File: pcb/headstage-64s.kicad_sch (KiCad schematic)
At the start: 8 parts, among them J1 Conn_Coaxial, J2 DF40C-70DP-0.4V(51)

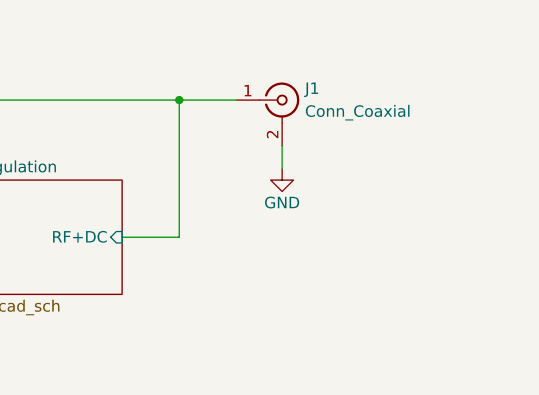
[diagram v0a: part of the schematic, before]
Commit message: Rev. A initial design prior to fab comments
- BOM simplification
- Added my initials to the board
- Made the board more easy to panlize
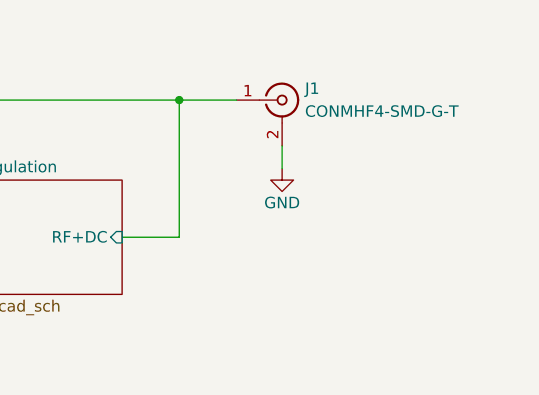
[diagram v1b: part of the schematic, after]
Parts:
- J1: value Conn_Coaxial -> CONMHF4-SMD-G-T; footprint jonnew:LINX_CONMHF4-SMD-G -> Headstage-64s:Coax-Adapter
- TP2: now left out of the parts list
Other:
- title: Headstage-RHS2116 -> Headstage-64s
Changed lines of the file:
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@@
   (paper "A4" portrait)
   (title_block
-    (title "Headstage-RHS2116")
-    (date "2021-12-16")
+    (title "Headstage-64s")
+    (date "2022-01-21")
     (rev "A")
     (company "Open Ephys, Inc")
@@
   )
   (symbol (lib_id "Connector:TestPoint") (at 52.07 60.96 0) (unit 1)
-    (in_bom yes) (on_board yes)
+    (in_bom no) (on_board yes)
     (property "Reference" "TP2" (id 0) (at 53.34 58.42 0)
       (effects (font (size 1.27 1.27)) (justify left))
@@
       (effects (font (size 1.27 1.27)) (justify left))
     )
-    (property "Value" "Conn_Coaxial" (id 1) (at 163.83 54.61 0)
-      (effects (font (size 1.27 1.27)) (justify left))
-    )
-    (property "Footprint" "jonnew:LINX_CONMHF4-SMD-G" (id 2) (at 161.29 53.34 0)
+    (property "Value" "CONMHF4-SMD-G-T" (id 1) (at 163.83 54.61 0)
+      (effects (font (size 1.27 1.27)) (justify left))
+    )
+    (property "Footprint" "Headstage-64s:Coax-Adapter" (id 2) (at 161.29 53.34 0)
       (effects (font (size 1.27 1.27)) hide)
     )
@@
       (reference "#PWR02") (unit 1) (value "+3.3V") (footprint "")
     )
+    (path "/ef67450c-7896-4369-9f65-a6a0bf770996/c8f58c2d-07ec-4355-92b4-a1615dc2f910"
+      (reference "#PWR03") (unit 1) (value "GND") (footprint "")
+    )
+    (path "/ef67450c-7896-4369-9f65-a6a0bf770996/21a98fd8-a677-4041-a72a-fa16dabfe8d3"
+      (reference "#PWR04") (unit 1) (value "+1V8") (footprint "")
+    )
     (path "/f805e42a-7731-4c63-aab8-b693117b73f1/f96f902c-692c-4845-9eef-cc912aa845ab"
       (reference "#PWR017") (unit 1) (value "GND") (footprint "")
@@
     )
     (path "/ef67450c-7896-4369-9f65-a6a0bf770996/111e9f78-ceab-42c3-b66c-e2ed604ec711"
-      (reference "C51") (unit 1) (value "1.0uF") (footprint "Capacitor_SMD:C_0402_1005Metric")
+      (reference "C51") (unit 1) (value "1uF") (footprint "Capacitor_SMD:C_0402_1005Metric")
     )
     (path "/ef67450c-7896-4369-9f65-a6a0bf770996/2b42fc13-7e16-4022-9298-19773a99f7dc"
-      (reference "C52") (unit 1) (value "1.0uF") (footprint "Capacitor_SMD:C_0402_1005Metric")
+      (reference "C52") (unit 1) (value "1uF") (footprint "Capacitor_SMD:C_0402_1005Metric")
     )
     (path "/ef67450c-7896-4369-9f65-a6a0bf770996/fcee6037-f9fd-4eff-9d73-c32d97d31ae2"
@@
     )
     (path "/ef67450c-7896-4369-9f65-a6a0bf770996/55545dfc-6930-4e99-9286-8901835b1e37"
-      (reference "D2") (unit 1) (value "LED") (footprint "jonnew:ROHM_SML-P11MTT86R")
+      (reference "D2") (unit 1) (value "SML-P11UTT86R") (footprint "jonnew:ROHM_SML-P11MTT86R")
     )
     (path "/ec2eb303-8bda-4887-86fa-cfe7bb147514/5e9fe99d-ee33-41ec-b2ff-8866abf981ee"
@@
     )
     (path "/9086d3ed-d48c-44a7-83ea-71ce6fdb9e26"
-      (reference "J1") (unit 1) (value "Conn_Coaxial") (footprint "jonnew:LINX_CONMHF4-SMD-G")
+      (reference "J1") (unit 1) (value "CONMHF4-SMD-G-T") (footprint "Headstage-64s:Coax-Adapter")
     )
     (path "/fccc0e4f-ed50-4339-ad4b-4dd5485914e2"
       (reference "J2") (unit 1) (value "DF40C-70DP-0.4V(51)") (footprint "jonnew:HIROSE_DF40C70DP04V51")
     )
+    (path "/ef67450c-7896-4369-9f65-a6a0bf770996/d1a6949e-04d4-4c1c-b488-f7d497860452"
+      (reference "J3") (unit 1) (value "SBH11-PBPC-D05-ST-BK") (footprint "Connector_IDC:IDC-Header_2x05_P2.54mm_Vertical")
+    )
     (path "/ef67450c-7896-4369-9f65-a6a0bf770996/b1fef073-48b9-4936-be2b-7ec71e5f6dd4"
       (reference "J5") (unit 1) (value "PINHD-1x7_ONIXJTAG-RevA") (footprint "jonnew:ONIXJTAG-RevA")
     )
+    (path "/ef67450c-7896-4369-9f65-a6a0bf770996/4a2bdb04-11f3-4675-8736-8b6d29b5959b"
+      (reference "JP1") (unit 1) (value "Jumper_2_Open") (footprint "jonnew:OE_SolderJumper-2_0201_Open_Pad")
+    )
     (path "/6a107470-4fd1-4a6d-84fa-4453722c41a9/63ea2017-127c-47a0-ae03-040ce3a6283c"
       (reference "L1") (unit 1) (value "BLM15AX102SN1D") (footprint "Inductor_SMD:L_0402_1005Metric")
@@
     )
     (path "/6a107470-4fd1-4a6d-84fa-4453722c41a9/a20bf941-be10-4b9f-bf67-16c9e833102b"
-      (reference "R3") (unit 1) (value "?") (footprint "Resistor_SMD:R_0201_0603Metric")
+      (reference "R3") (unit 1) (value "39.2,1%") (footprint "Resistor_SMD:R_0201_0603Metric")
     )
     (path "/6a107470-4fd1-4a6d-84fa-4453722c41a9/66966924-f4e3-42e3-b604-4f625989070c"
-      (reference "R4") (unit 1) (value "?") (footprint "Resistor_SMD:R_0201_0603Metric")
+      (reference "R4") (unit 1) (value "78.7k,1%") (footprint "Resistor_SMD:R_0201_0603Metric")
     )
     (path "/6a107470-4fd1-4a6d-84fa-4453722c41a9/8f2ed134-eb1d-4a2c-b225-1ddae1540dc0"
@@
     )
     (path "/6a107470-4fd1-4a6d-84fa-4453722c41a9/b7fbf054-a4bb-464c-87a8-918d57bd9d6d"
-      (reference "R6") (unit 1) (value "?") (footprint "Resistor_SMD:R_0201_0603Metric")
+      (reference "R6") (unit 1) (value "40.2k,1%") (footprint "Resistor_SMD:R_0201_0603Metric")
     )
     (path "/f805e42a-7731-4c63-aab8-b693117b73f1/9bdb9eb7-4e1a-4718-a0a3-e80ccfd63967"

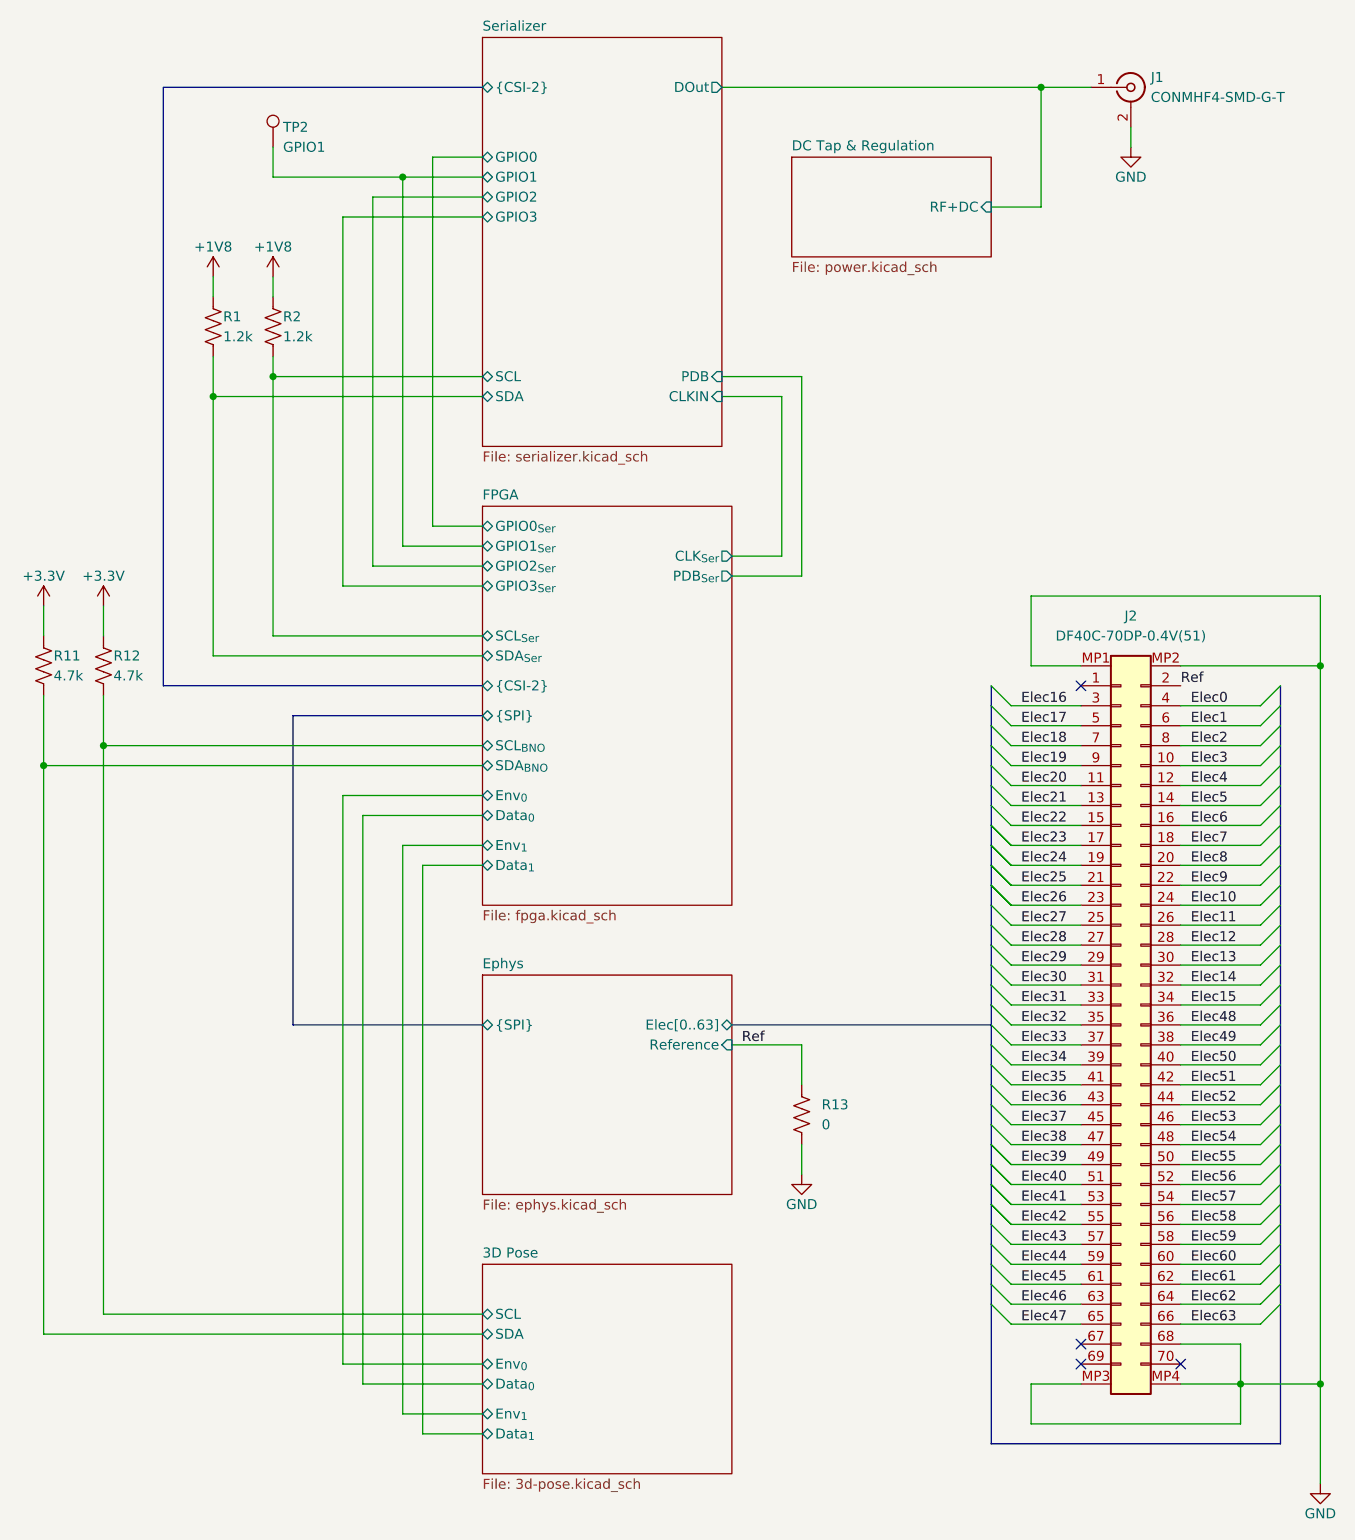
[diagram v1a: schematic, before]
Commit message: Small changes before speedy fabrication
- This is revision A
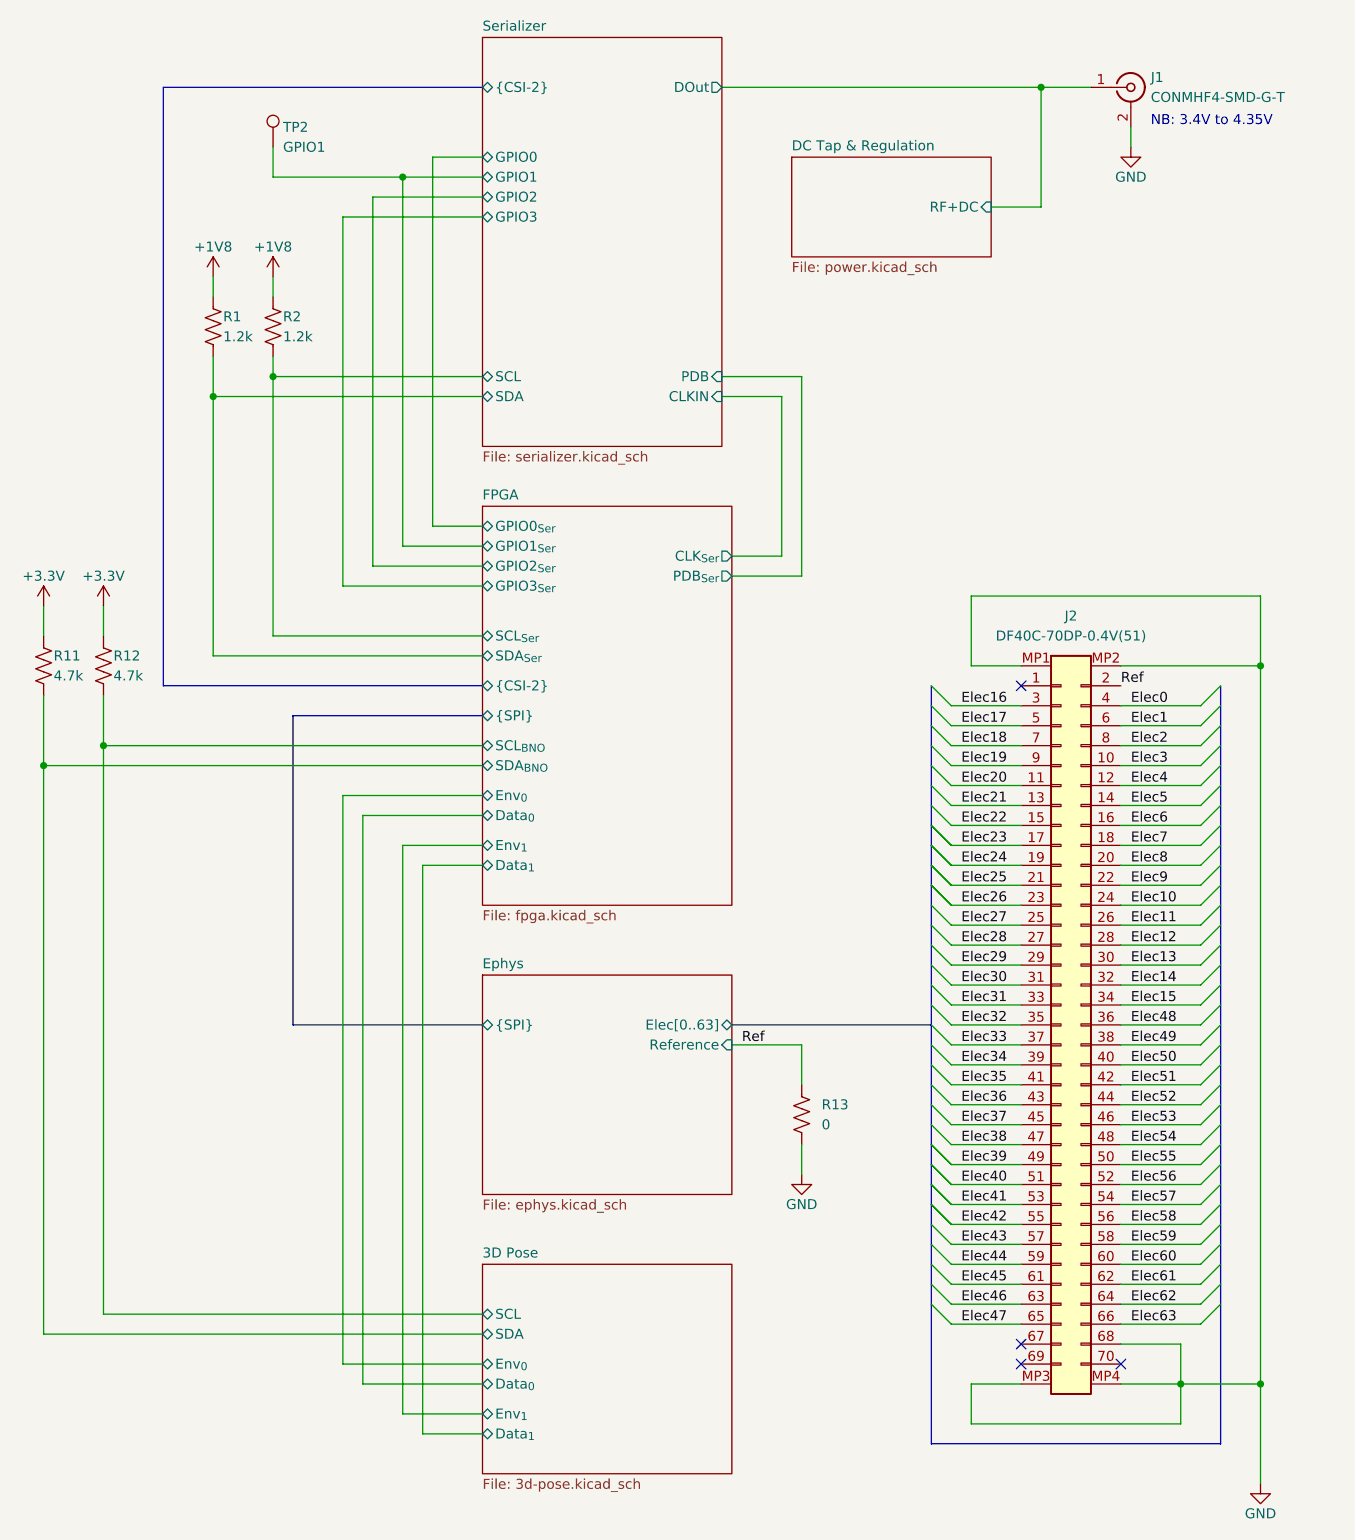
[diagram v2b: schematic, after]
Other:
- note added: "NB: 3.4V to 4.35V"
- moved on the sheet: J2

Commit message: Start of revision B
- Address the following issues
1. The photodiode anode is on pin 3, not pin 2
2. No paste on coax connector
3. CRESET_B needs to come out to programming header
4. Need PU on CS line.
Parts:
- J1, TP2: DNP (none) -> DNP
- R1, R2: value 1.2k -> 1k
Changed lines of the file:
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@@
     (title "Headstage-64s")
     (date "2022-01-21")
-    (rev "A")
+    (rev "B")
     (company "Open Ephys, Inc")
     (comment 1 "Jonathan P. Newman")
@@
       (effects (font (size 1.27 1.27)) hide)
     )
+    (property "DNP" "DNP" (id 4) (at 52.07 60.96 0)
+      (effects (font (size 1.27 1.27)) hide)
+    )
     (pin "1")
   )
@@
       (effects (font (size 1.27 1.27)) (justify left))
     )
-    (property "Value" "1.2k" (id 1) (at 45.72 85.09 0)
+    (property "Value" "1k" (id 1) (at 45.72 85.09 0)
       (effects (font (size 1.27 1.27)) (justify left))
     )
@@
       (effects (font (size 1.27 1.27)) hide)
     )
-    (property "Datasheet" " ~" (id 3) (at 161.29 53.34 0)
+    (property "Datasheet" "~" (id 3) (at 161.29 53.34 0)
+      (effects (font (size 1.27 1.27)) hide)
+    )
+    (property "DNP" "DNP" (id 4) (at 161.29 53.34 0)
       (effects (font (size 1.27 1.27)) hide)
     )
@@
       (effects (font (size 1.27 1.27)) (justify left))
     )
-    (property "Value" "1.2k" (id 1) (at 53.34 85.09 0)
+    (property "Value" "1k" (id 1) (at 53.34 85.09 0)
       (effects (font (size 1.27 1.27)) (justify left))
     )
@@
       (effects (font (size 1.27 1.27)) hide)
     )
-    (property "Datasheet" "" (id 3) (at 153.67 124.46 0)
+    (property "Datasheet" "~" (id 3) (at 153.67 124.46 0)
       (effects (font (size 1.27 1.27)) hide)
     )
@@
       (reference "#PWR04") (unit 1) (value "+1V8") (footprint "")
     )
+    (path "/ef67450c-7896-4369-9f65-a6a0bf770996/819931e3-3585-408b-b9ce-37068f05fc30"
+      (reference "#PWR05") (unit 1) (value "+1V8") (footprint "")
+    )
     (path "/f805e42a-7731-4c63-aab8-b693117b73f1/f96f902c-692c-4845-9eef-cc912aa845ab"
       (reference "#PWR017") (unit 1) (value "GND") (footprint "")
@@
       (reference "C58") (unit 1) (value "10nF") (footprint "Capacitor_SMD:C_0201_0603Metric")
     )
-    (path "/ec2eb303-8bda-4887-86fa-cfe7bb147514/8b53894d-0827-4c6c-80ee-929ae109ec5d"
+    (path "/ec2eb303-8bda-4887-86fa-cfe7bb147514/8828788e-df99-49a3-821d-754234d6a54f"
       (reference "D1") (unit 1) (value "SFH 2400 FA") (footprint "jonnew:OSRAM_SFH2400FA-Tight")
     )
@@
       (reference "D2") (unit 1) (value "SML-P11UTT86R") (footprint "jonnew:ROHM_SML-P11MTT86R")
     )
-    (path "/ec2eb303-8bda-4887-86fa-cfe7bb147514/5e9fe99d-ee33-41ec-b2ff-8866abf981ee"
+    (path "/ec2eb303-8bda-4887-86fa-cfe7bb147514/212d31ef-d376-4be8-ad3b-957dae694691"
       (reference "D3") (unit 1) (value "SFH 2400 FA") (footprint "jonnew:OSRAM_SFH2400FA-Tight")
     )
@@
     )
     (path "/5fd7a87f-1f66-4a0e-9170-a3d4b87e664e"
-      (reference "R1") (unit 1) (value "1.2k") (footprint "Resistor_SMD:R_0201_0603Metric")
+      (reference "R1") (unit 1) (value "1k") (footprint "Resistor_SMD:R_0201_0603Metric")
     )
     (path "/ca30b210-3b4a-4e7a-930d-73fceb3e3f65"
-      (reference "R2") (unit 1) (value "1.2k") (footprint "Resistor_SMD:R_0201_0603Metric")
+      (reference "R2") (unit 1) (value "1k") (footprint "Resistor_SMD:R_0201_0603Metric")
     )
     (path "/6a107470-4fd1-4a6d-84fa-4453722c41a9/a20bf941-be10-4b9f-bf67-16c9e833102b"
@@
       (reference "R13") (unit 1) (value "0") (footprint "Resistor_SMD:R_0201_0603Metric")
     )
+    (path "/ef67450c-7896-4369-9f65-a6a0bf770996/b4c41f79-0a04-4604-931c-c773f97e5d47"
+      (reference "R14") (unit 1) (value "4.7k") (footprint "Resistor_SMD:R_0201_0603Metric")
+    )
     (path "/6a107470-4fd1-4a6d-84fa-4453722c41a9/7cee0d83-c827-4c1a-ad50-83af50d892c9"
